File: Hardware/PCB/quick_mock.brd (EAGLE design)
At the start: 99.1 x 99.1 mm, 24 parts

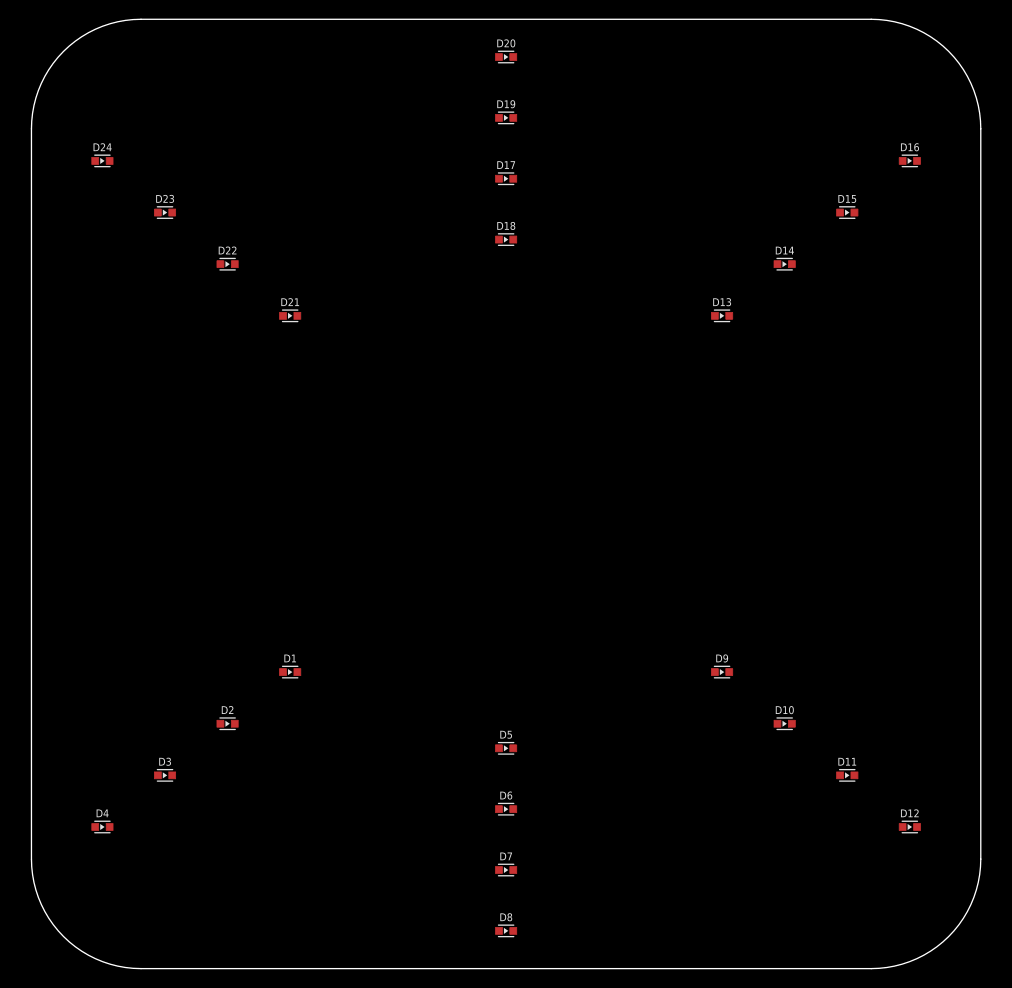
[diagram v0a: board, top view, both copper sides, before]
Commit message: add lenses to housing. update PCB dimensions and cutouts to match.
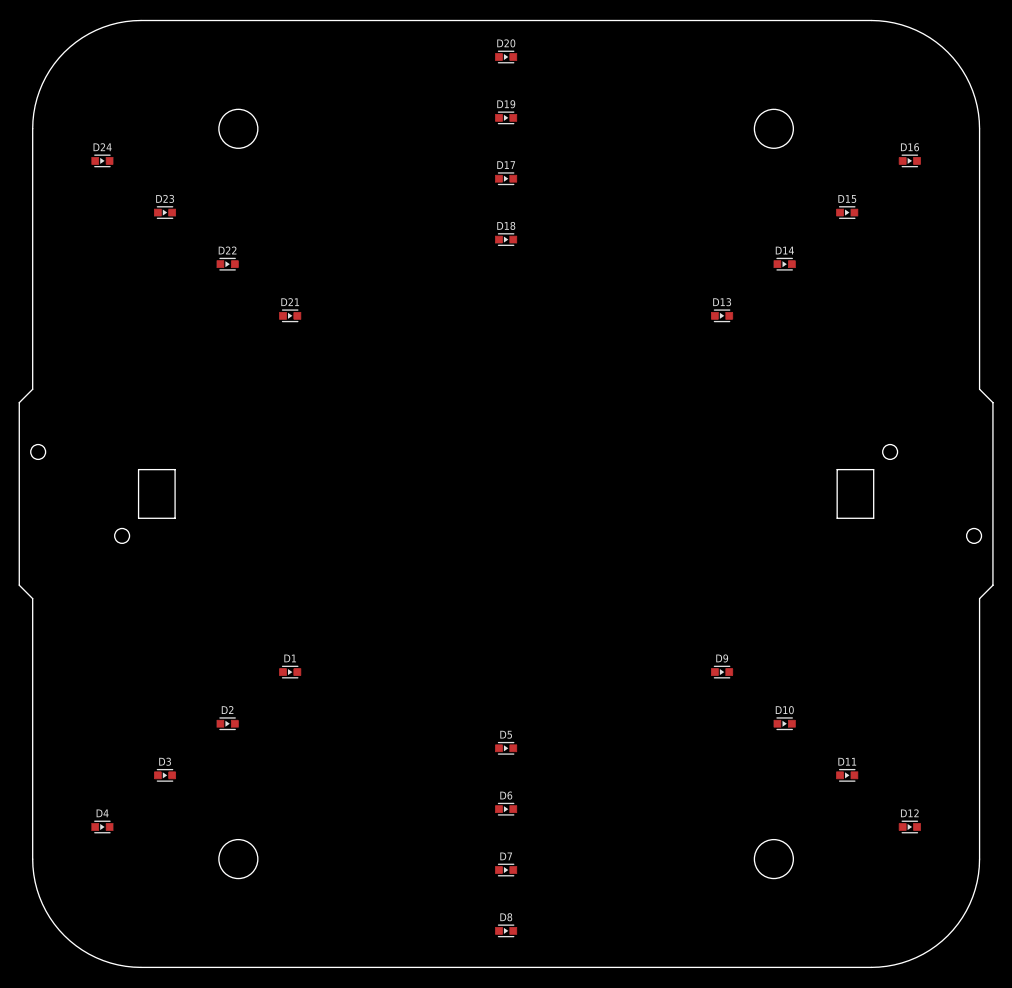
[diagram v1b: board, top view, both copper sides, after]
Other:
- board size 99.1 x 99.1 mm -> 101.6 x 98.8 mm
- board text added: "Receiver"
- board text added: "Transmitter"

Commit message: adjust hole sizes. replace emitter LEDs
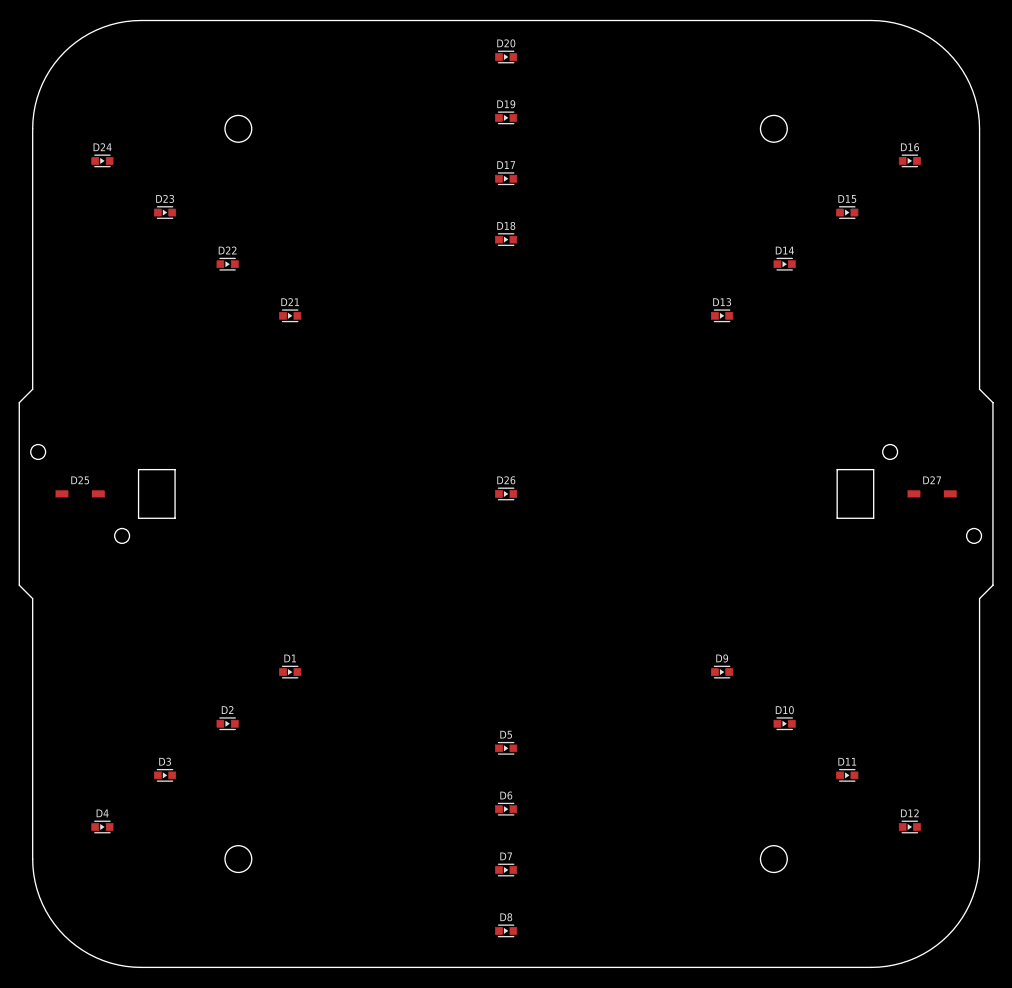
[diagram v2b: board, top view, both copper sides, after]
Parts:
- added D25, D27: VSMB2020X01, Rob-Diodes:GULL-WING-2.3MM
- added D26: LED-603, Rob-Diodes:SMD-603
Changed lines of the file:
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@@
 </layers>
 <board>
-<fusionsync huburn="a.YnVzaW5lc3M6c3VuZGJlcmdmZXJhcg" projecturn="a.YnVzaW5lc3M6c3VuZGJlcmdmZXJhciMyMDIyMDkwNjU1MzEzMzI4MQ" f3durn="urn:adsk.wipprod:dm.lineage:_LBjbpjSReejQ1QNtJxQtQ" pcbguid="" lastpulledtime="" lastsyncedchangeguid="" latestrevisionid="f5b60855-6e7b-4d74-8156-d1332458dd38" lastsyncedrevisionid="f5b60855-6e7b-4d74-8156-d1332458dd38" lastboardhashguid="b8e310b4-e6ef-eddc-2d3b-9480b213e5a7" lastpushedtime="2023-02-28T01:28:50Z" linktopcb3d="true"/>
+<fusionsync huburn="a.YnVzaW5lc3M6c3VuZGJlcmdmZXJhcg" projecturn="a.YnVzaW5lc3M6c3VuZGJlcmdmZXJhciMyMDIyMDkwNjU1MzEzMzI4MQ" f3durn="urn:adsk.wipprod:dm.lineage:_LBjbpjSReejQ1QNtJxQtQ" pcbguid="" lastpulledtime="" lastsyncedchangeguid="" latestrevisionid="c8c15753-8cb0-4c92-aaa7-c8cb3c30b25e" lastsyncedrevisionid="c8c15753-8cb0-4c92-aaa7-c8cb3c30b25e" lastboardhashguid="f6b63956-15fd-f67c-a3b4-4bf64a7ab889" lastpushedtime="2023-03-03T02:30:11Z" linktopcb3d="true"/>
 <plain>
 <wire x1="53.975" y1="24.695375" x2="53.88615625" y2="25.113003125" width="0" layer="49"/>
@@
 <wire x1="0" y1="41.275" x2="0" y2="60.325" width="0.0254" layer="20"/>
 <wire x1="0" y1="60.325" x2="1.397" y2="61.722" width="0.0254" layer="20"/>
-<hole x="22.86" y="88.9" drill="4.064"/>
-<hole x="78.74" y="88.9" drill="4.064"/>
-<hole x="78.74" y="12.7" drill="4.064"/>
-<hole x="22.86" y="12.7" drill="4.064"/>
+<hole x="22.86" y="88.9" drill="2.794"/>
+<hole x="78.74" y="88.9" drill="2.794"/>
+<hole x="78.74" y="12.7" drill="2.794"/>
+<hole x="22.86" y="12.7" drill="2.794"/>
 <hole x="1.97" y="55.18" drill="1.55"/>
 <hole x="99.63" y="46.42" drill="1.55"/>
@@
 <attribute name="VALUE" x="8.6741" y="84.53628125" size="0.8128" layer="27" font="vector" ratio="12" align="top-center"/>
 </element>
+<element name="D25" library="Rob-Diodes" library_urn="urn:adsk.eagle:library:37150039" package="GULL-WING-2.3MM" package3d_urn="urn:adsk.eagle:package:39410737/2" value="VSMB2020X01" x="6.35" y="50.8" smashed="yes">
+<attribute name="NAME" x="6.35" y="51.816" size="0.8128" layer="25" font="vector" ratio="12" align="bottom-center"/>
+<attribute name="VALUE" x="6.35" y="49.784" size="0.8128" layer="27" font="vector" ratio="12" align="top-center"/>
+</element>
+<element name="D26" library="Rob-Diodes" library_urn="urn:adsk.eagle:library:37150039" package="SMD-603" package3d_urn="urn:adsk.eagle:package:37041000/3" value="LED-603" x="50.8" y="50.8" smashed="yes">
+<attribute name="NAME" x="50.8" y="51.816" size="0.8128" layer="25" font="vector" ratio="12" align="bottom-center"/>
+<attribute name="VALUE" x="50.8" y="49.784" size="0.8128" layer="27" font="vector" ratio="12" align="top-center"/>
+</element>
+<element name="D27" library="Rob-Diodes" library_urn="urn:adsk.eagle:library:37150039" package="GULL-WING-2.3MM" package3d_urn="urn:adsk.eagle:package:39410737/2" value="VSMB2020X01" x="95.25" y="50.8" smashed="yes">
+<attribute name="NAME" x="95.25" y="51.816" size="0.8128" layer="25" font="vector" ratio="12" align="bottom-center"/>
+<attribute name="VALUE" x="95.25" y="49.784" size="0.8128" layer="27" font="vector" ratio="12" align="top-center"/>
+</element>
 </elements>
